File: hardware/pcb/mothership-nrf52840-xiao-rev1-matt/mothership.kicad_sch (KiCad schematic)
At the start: 30 parts, among them J1 HRO TYPE-C-31-M-12, J2 USB_EXT_FFC_CABLE, J3 Screw_Terminal_01x01, J4 BOT_L, J5 BOT_R, J6 TOP_R, J7 TOP_L, J8 SPI, J9 EC11, Q1 AO3401A, SW1 SW_SPDT_321, U1 NCP361SN, U2 XIAO_nRF52840, U3 MCP23017x-x-SS, U4 MCP23017x-x-SS, U5 DT1452-02SO

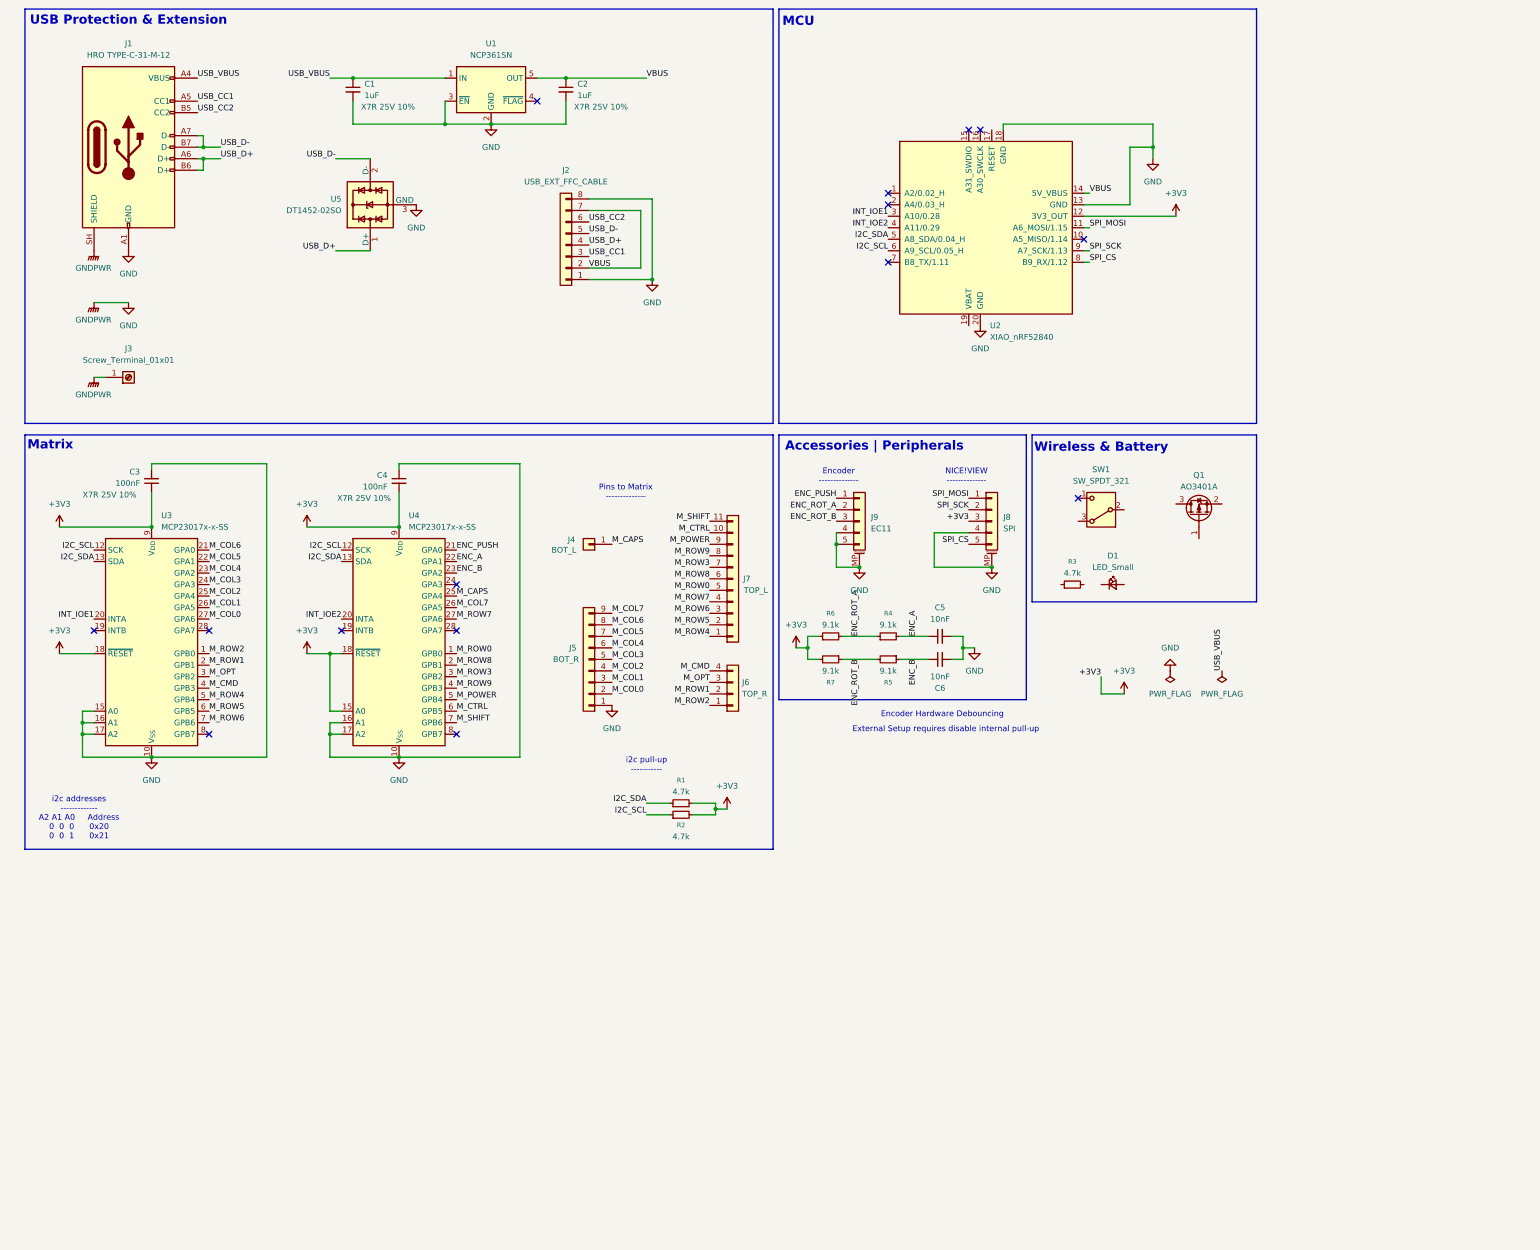
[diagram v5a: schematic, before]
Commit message: pcb|sch: complete initial prototype schema
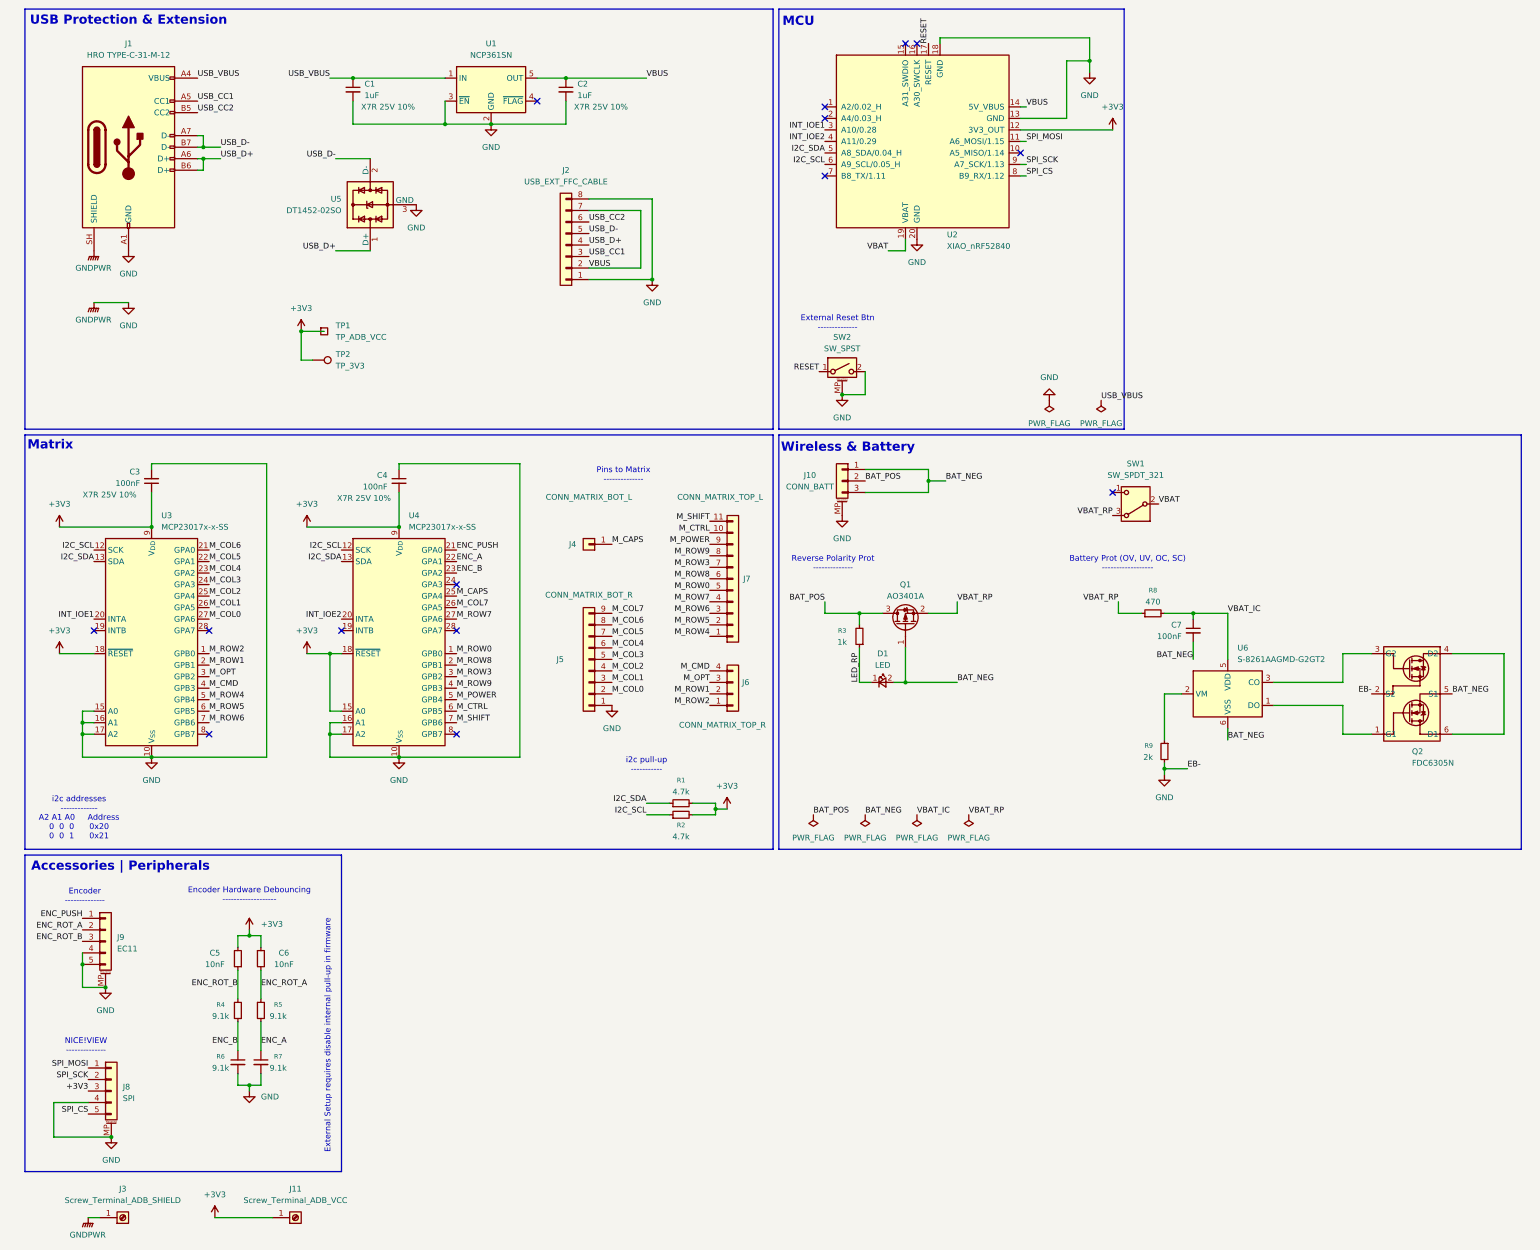
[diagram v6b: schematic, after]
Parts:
- added C7: 100nF, A9M0330:Capacitor_SMD__C_0603_1608Metric_Pad1.08x0.95mm_HandSolder, symbol A9M0330:C_Small
- added J10: CONN_BATT, A9M0330:Conn_Hirose__DF3-3P-2DS_1x03_P2.00mm_Horizontal, symbol A9M0330:Conn_01x03_MountingPin
- added J11: Screw_Terminal_ADB_VCC, A9M0330:MountingHole_2.7mm_M2.5_Pad_Via, symbol A9M0330:Screw_Terminal_01x01
- added Q2: FDC6305N, A9M0330:TO_SOT_SMD__TSOT-23-6_ON, symbol A9M0330:Transition_FET__FDC6305N
- added R8: 470, A9M0330:Resistor_SMD__R_0603_1608Metric_Pad0.98x0.95mm_HandSolder, symbol A9M0330:R_Small
- added R9: 2k, A9M0330:Resistor_SMD__R_0603_1608Metric_Pad0.98x0.95mm_HandSolder, symbol A9M0330:R_Small
- added SW2: SW_SPST, A9M0330:SW_SPDT_SMD__Slide_321_Shouhan_MINI_MSK12C02__Mounting_AnchorVias, symbol A9M0330:SW_SPST_MountingPin
- added TP1: TP_ADB_VCC, symbol A9M0330:TestPoint_Square
- added TP2: TP_3V3, symbol A9M0330:TestPoint
- added U6: S-8261AAGMD-G2GT2, A9M0330:TO_SOT_SMD__SOT-23-6_MP006-A, symbol A9M0330:Battery_Management__Protection_IC_Ablic_S-8240ADQ-M6T1U
- C1, C2, C3, C4, C5, C6: footprint (none) -> A9M0330:Capacitor_SMD__C_0603_1608Metric_Pad1.08x0.95mm_HandSolder
- D1: value LED_Small -> LED
- J1: footprint (none) -> A9M0330:USB_C_Receptacle__16P_HRO_TYPE-C-31-M-12_HandSolder
- J3: value Screw_Terminal_01x01 -> Screw_Terminal_ADB_SHIELD; footprint (none) -> A9M0330:MountingHole_2.7mm_M2.5_Pad_Via
- J4: value BOT_L -> CONN_MATRIX_BOT_L
- J5: value BOT_R -> CONN_MATRIX_BOT_R
- J6: value TOP_R -> CONN_MATRIX_TOP_R
- J7: value TOP_L -> CONN_MATRIX_TOP_L
- Q1: footprint Package_TO_SOT_SMD:SOT-23 -> A9M0330:TO_SOT_SMD__SOT-23-3_AOS
- R1, R2, R4, R5, R6, R7: footprint (none) -> A9M0330:Resistor_SMD__R_0603_1608Metric_Pad0.98x0.95mm_HandSolder
- R3: value 4.7k -> 1k; footprint (none) -> A9M0330:Resistor_SMD__R_0603_1608Metric_Pad0.98x0.95mm_HandSolder
- SW1: footprint (none) -> A9M0330:SW_SPDT_SMD__Slide_321_Shouhan_MINI_MSK12C02__Mounting_AnchorVias
- U1: footprint Package_SO:TSOP-5_1.65x3.05mm_P0.95mm -> A9M0330:SO__TSOP-5_1.65x3.05mm_P0.95mm_ON
- U3, U4: footprint Package_SO:SSOP-28_5.3x10.2mm_P0.65mm -> A9M0330:SO__SSOP-28_5.3x10.2mm_P0.65mm
- U5: footprint Package_TO_SOT_SMD:SOT-23 -> A9M0330:TO_SOT_SMD__SOT-23_DIO
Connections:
- net +3V3: now also J11.1 (Pin_1), TP1.1, TP2.1
- net GND: now also J10.MP (MountPin), Q2.2 (S2), R9.2, SW2.2 (B), SW2.MP (MountPin)
- net BAT_NEG: now reaches Q1.1 (G)
- net BAT_NEG: now also D1.2 (A), C7.2, J10.1 (Pin_1), J10.3 (Pin_3), Q2.5 (S1), U6.6 (VSS)
- net VBAT_RP: now reaches Q1.2 (S)
- net VBAT_RP: now also SW1.3 (A), R8.1
- net BAT_POS: now reaches Q1.3 (D)
- net BAT_POS: now also R3.2, J10.2 (Pin_2)
- net RESET: now reaches U2.17 (RESET)
- net RESET: now also SW2.1 (A)
- net VBAT: now reaches U2.19 (VBAT)
- net VBAT: now also SW1.2 (B)
- net LED_RP: now reaches R3.1
- net LED_RP: now also D1.1 (K)
- new net: Q2.1 (G1), U6.1 (DO)
- new net: Q2.3 (G2), U6.3 (CO)
- new net: Q2.4 (D2), Q2.6 (D1)
- new net: R9.1, U6.2 (VM)
- new net VBAT_IC: C7.1, R8.2, U6.5 (VDD)
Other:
- note added: "Battery Prot (OV, UV, OC, SC) ------------------"
- note added: "Encoder Hardware Debouncing -------------------"
- note added: "External Reset Btn --------------"
- note added: "External Setup requires disable internal pull-up in firmware"
- note added: "Reverse Polarity Prot --------------"
- note removed: "Encoder Hardware Debouncing"
- note removed: "External Setup requires disable internal pull-up"
- moved on the sheet: C5, C6, J3, J8, J9, Q1, R3, R4, R5, R6, R7, SW1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

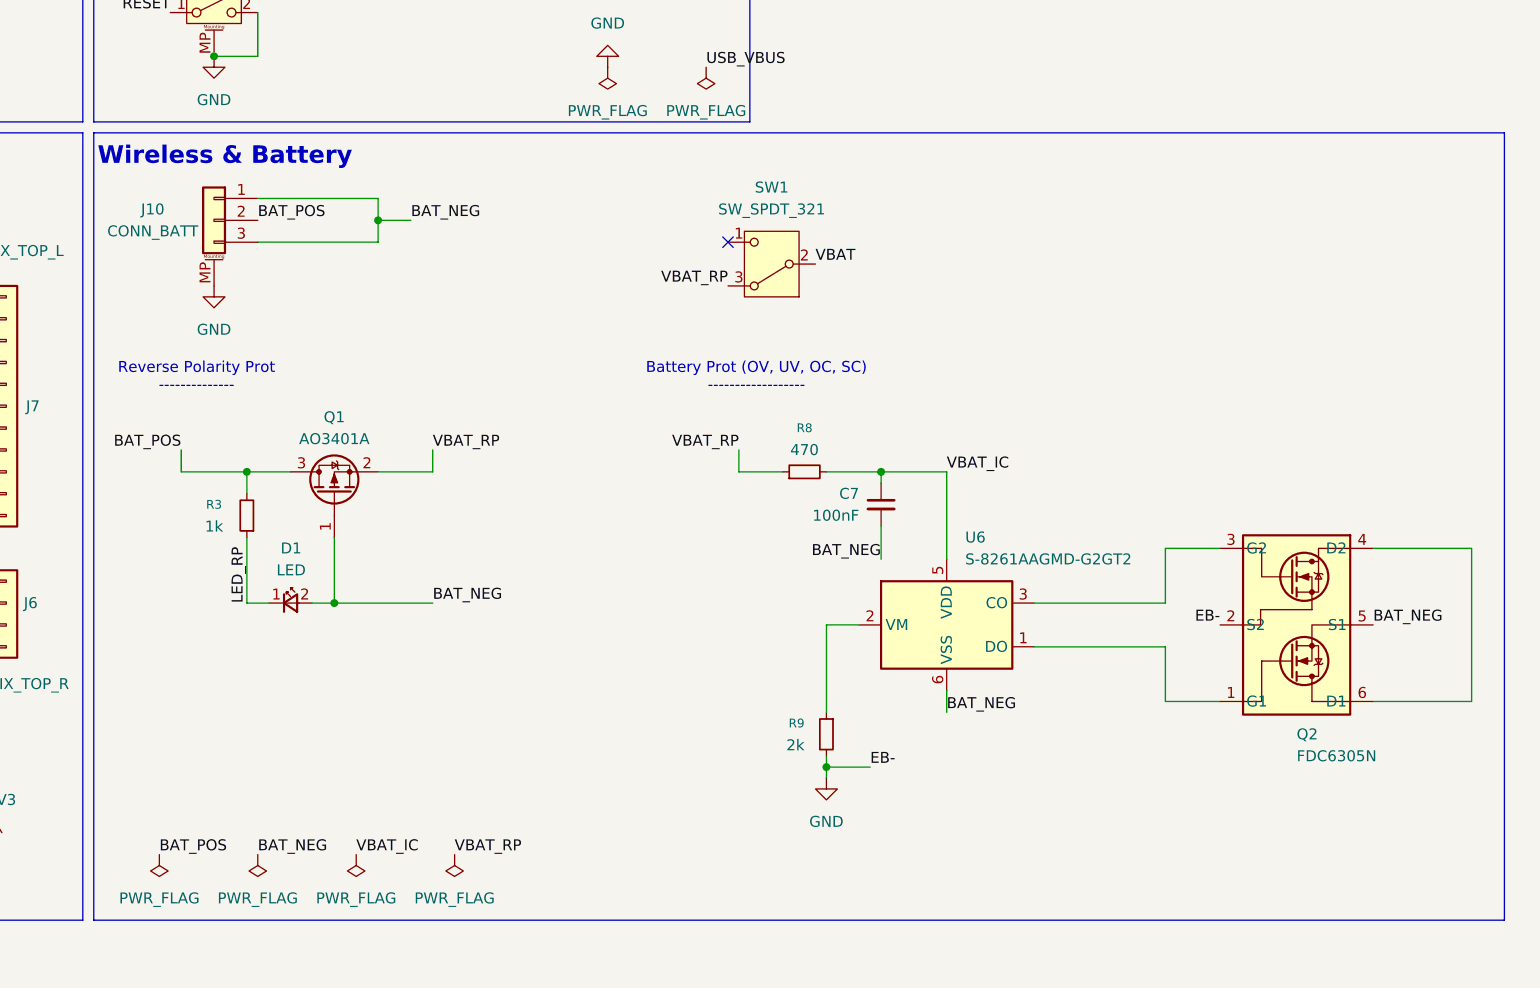
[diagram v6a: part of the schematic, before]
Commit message: sch: update configurations for bat ic protection
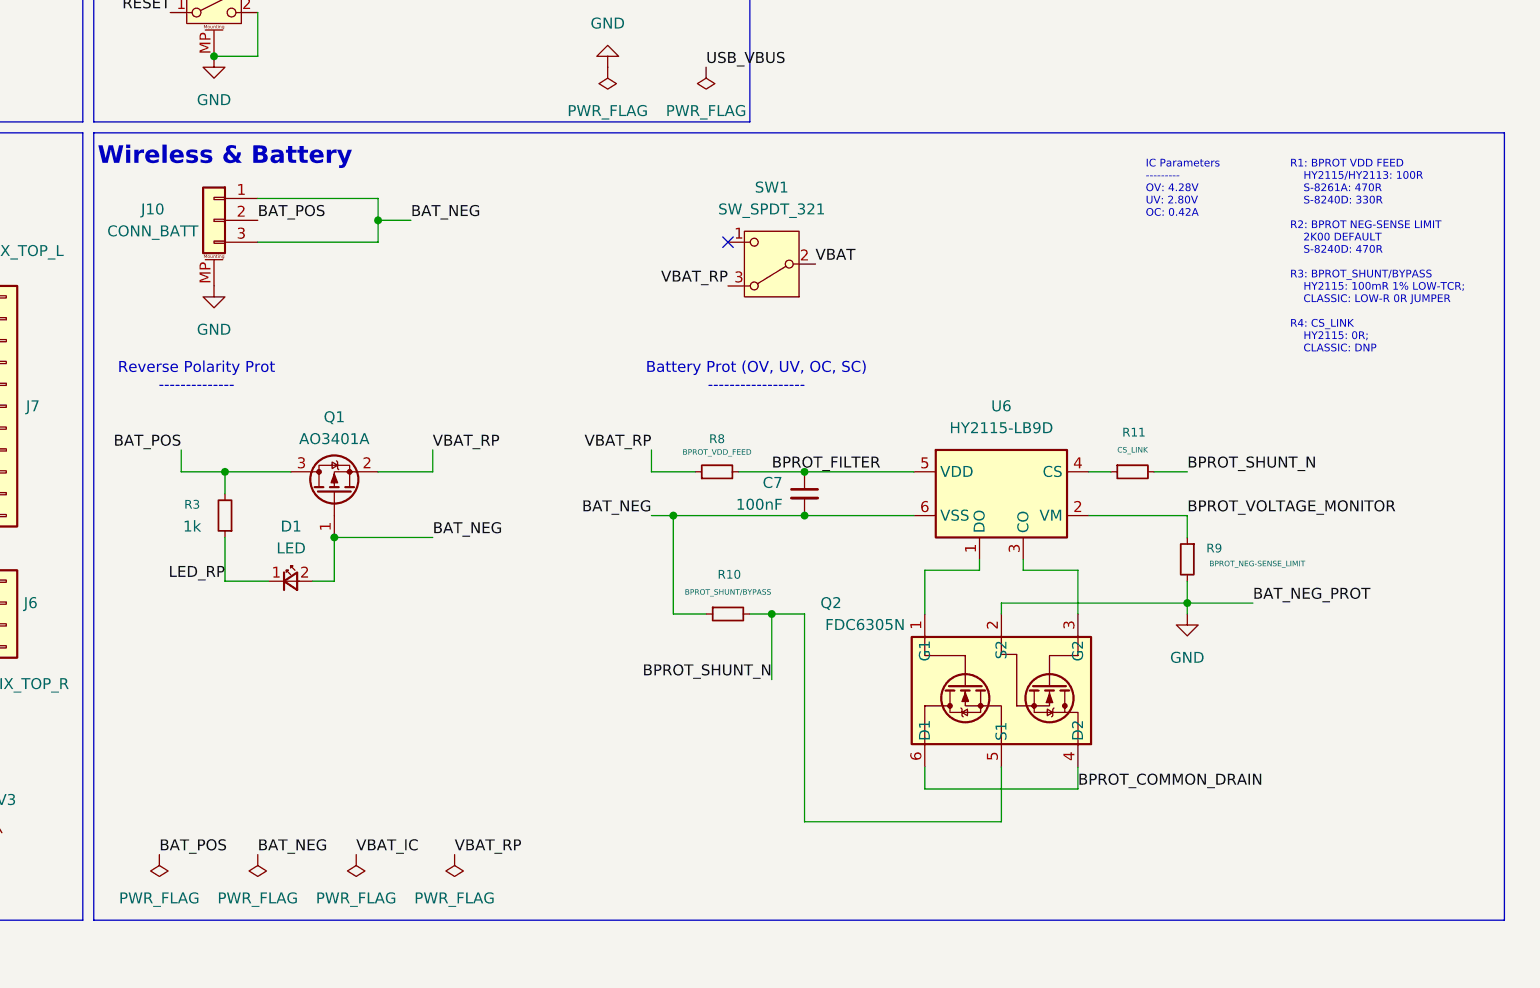
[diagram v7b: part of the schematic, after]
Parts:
- added R10: BPROT_SHUNT/BYPASS, A9M0330:Resistor_SMD__R_0603_1608Metric_Pad0.98x0.95mm_HandSolder, symbol A9M0330:R_Small
- added R11: CS_LINK, A9M0330:Resistor_SMD__R_0603_1608Metric_Pad0.98x0.95mm_HandSolder, symbol A9M0330:R_Small
- R8: value 470 -> BPROT_VDD_FEED
- R9: value 2k -> BPROT_NEG-SENSE_LIMIT
- U5: footprint A9M0330:TO_SOT_SMD__SOT-23_DIO -> Package_TO_SOT_SMD:SOT-23
- U6: value S-8261AAGMD-G2GT2 -> HY2115-LB9D; footprint A9M0330:TO_SOT_SMD__SOT-23-6_MP006-A -> Package_TO_SOT_SMD:SOT-23-6; symbol A9M0330:Battery_Management__Protection_IC_Ablic_S-8240ADQ-M6T1U -> A9M0330:Battery_Management__Protection_IC_HY2115; Alternative HYCON HY2113, Nisshinbo R5492 -> HYCON HY2115-LB9D
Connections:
- net BAT_NEG: now also R10.1; no longer Q2.5 (S1)
- net VBAT_IC: no longer C7.1, R8.2, U6.5 (VDD)
- net BPROT_COMMON_DRAIN: now reaches Q2.4 (D2), Q2.6 (D1)
- net BPROT_VOLTAGE_MONITOR: now reaches R9.1, U6.2 (VM)
- net at U6.4 (CS): now also R11.1
- new net BPROT_FILTER: C7.1, R8.2, U6.5 (VDD)
- new net BPROT_SHUNT_N: Q2.5 (S1), R10.2, R11.2
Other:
- note added: "IC Parameters --------- OV: 4.28V UV: 2.80V OC: 0.42A"
- note added: "R1: BPROT VDD FEED HY2115/HY2113: 100R S-8261A: 470R S-8240D: 330R R2: BPROT NEG-SENSE LIMIT 2K00 DEFAULT S-8240D: 470R R3: BPROT_SHUNT/BYPASS HY2115: 100mR 1% LOW-TCR; CLASSIC: LOW-R 0R JUMPER R4: CS_LINK HY2115: 0R; CLASSIC: DNP"
- moved on the sheet: C7, D1, R3, R8, R9
